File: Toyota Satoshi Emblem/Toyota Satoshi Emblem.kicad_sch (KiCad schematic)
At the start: 459 parts, among them J1 Conn_01x03_Male, J10 Conn_01x03_Male, J11 Letter Terminal, J12 Letter Terminal, J14 Power Port Terminal, J15 Raptor Term, J16 Serial Terminal, J17 S-Pads, J19 S-Pads, J2 Conn_01x03_Male, J20 S-Pads, J21 S-Pads, J22 Raptor Term, J23 Raptor Term, J24 Raptor Term, J3 Conn_01x03_Male, J4 Letter Terminal, J5 Letter Terminal, J6 Letter Terminal, J7 Letter Terminal, J8 Conn_01x03_Male, J9 Conn_01x03_Male, K1 FINDER-40.51, Q1 IRLR7843, Q10 IRLR7843, Q11 IRLR7843, Q12 2N3904, Q13 IRLR7843, Q14 IRLR7843, Q15 IRLR7843, Q16 2N3904, Q17 IRLR7843, Q18 IRLR7843, Q19 IRLR7843, Q2 IRLR7843, Q20 2N3904, Q21 IRLR7843, Q22 IRLR7843, Q23 IRLR7843, Q24 2N3904, Q25 IRLR7843, Q26 IRLR7843, Q27 IRLR7843, Q28 IRLR7843, Q29 IRLR7843, Q3 IRLR7843, Q30 IRLR7843, Q31 IRLR7843, Q32 IRLZ44N, Q33 IRLR7843, Q34 2N3904, Q35 IRLR7843, Q36 IRF4905, Q37 BC327, Q38 BC337, Q39 IRF4905, Q4 2N3904, Q5 IRLR7843, Q6 IRLR7843, Q7 IRLR7843, Q8 2N3904, Q9 IRLR7843, U5 L7805

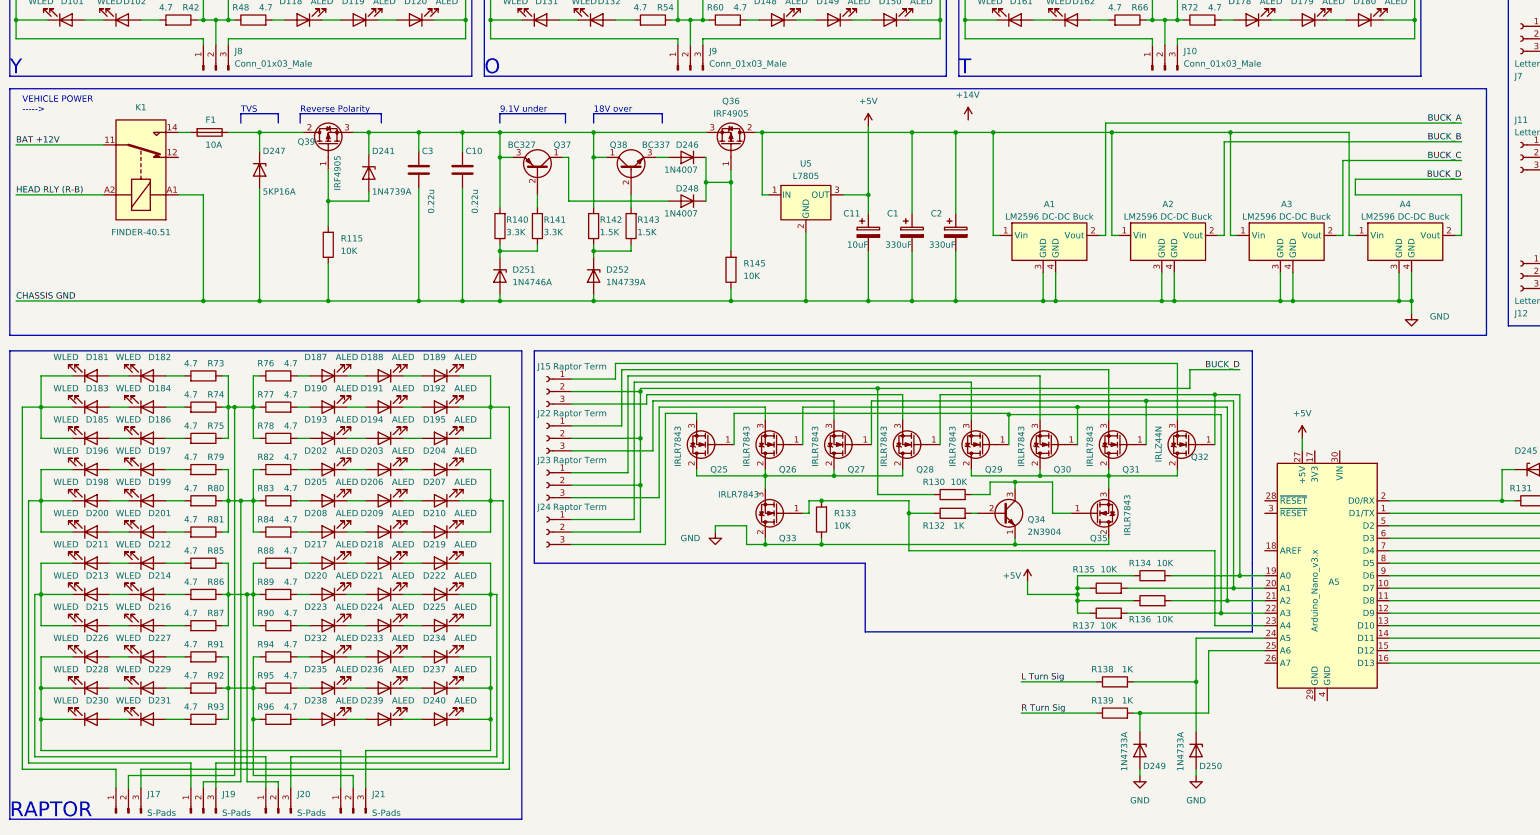
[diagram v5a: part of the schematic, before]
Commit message: v1.14
Control board pcb in the works
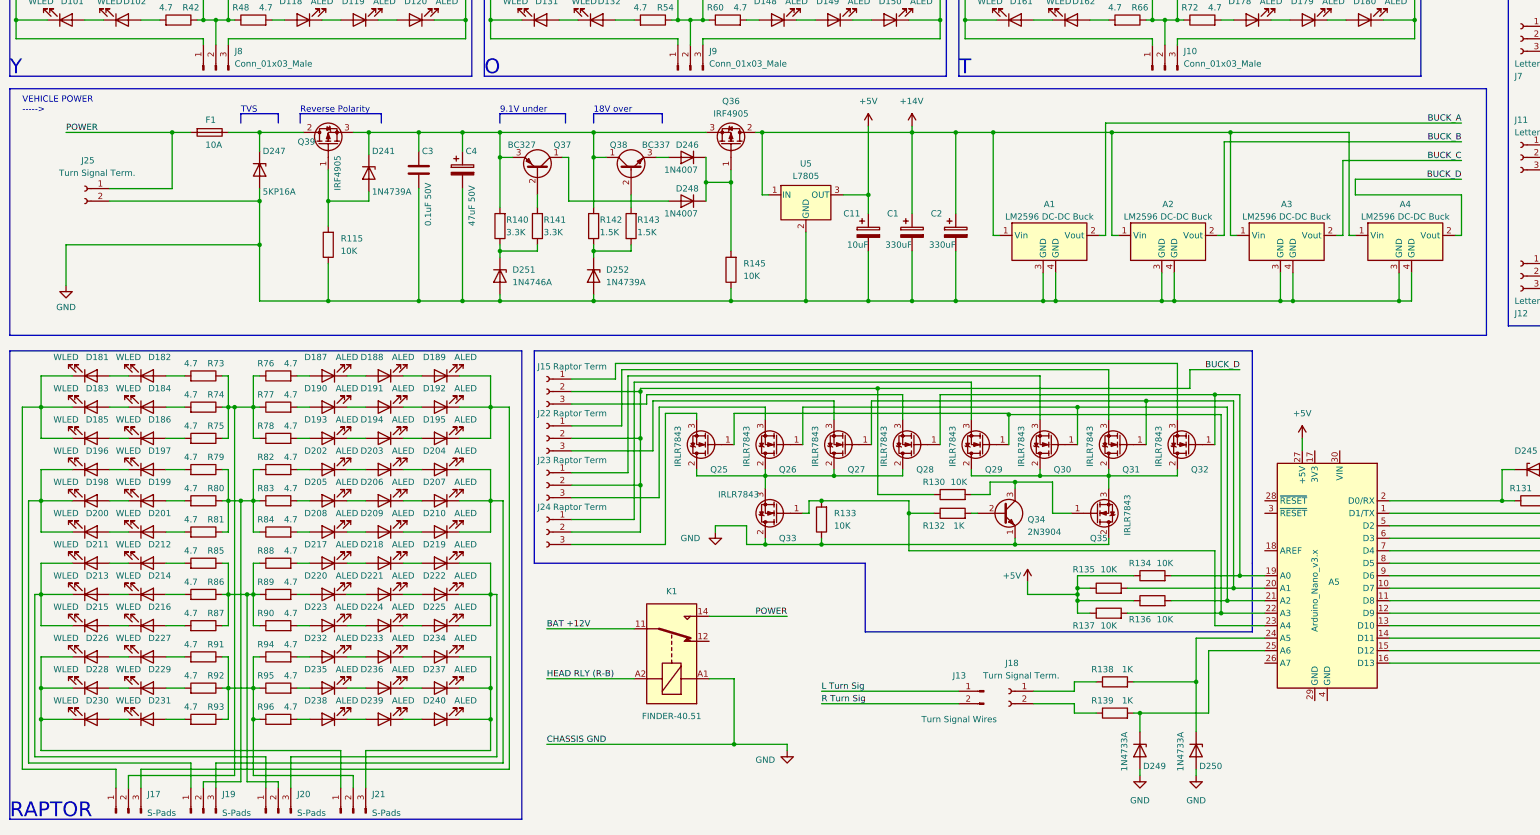
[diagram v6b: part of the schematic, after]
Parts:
- removed C10: 0.22u, symbol Device:C
- removed Q32: IRLZ44N, Package_TO_SOT_THT:TO-220-3_Vertical, symbol Transistor_FET:IRLZ44N
- added C4: 47uF 50V, Capacitor_THT:C_Radial_D5.0mm_H11.0mm_P2.00mm, symbol Device:C_Polarized
- added J13: Turn Signal Wires, TerminalBlock_Phoenix:TerminalBlock_Phoenix_MKDS-3-2-5.08_1x02_P5.08mm_Horizontal, symbol Connector:Conn_01x02_Male
- added J18, J25: Turn Signal Term., TerminalBlock_Phoenix:TerminalBlock_Phoenix_PT-1,5-2-5.0-H_1x02_P5.00mm_Horizontal, symbol Connector:Conn_01x02_Female
- added Q32: IRLR7843, afootprints:IRLR7843, symbol asymbols:IRLR7843
- C1, C2: footprint (none) -> Capacitor_THT:C_Radial_D8.0mm_H11.5mm_P3.50mm
- C11: footprint (none) -> Capacitor_THT:C_Radial_D4.0mm_H7.0mm_P1.50mm
- C3: value 0.22u -> 0.1uF 50V; footprint (none) -> Capacitor_THT:C_Disc_D7.5mm_W5.0mm_P5.00mm
- F1: footprint (none) -> afootprints:Univ_AUTO_Fuse
- J11, J12, J15, J22, J23, J24, J4, J5, J6, J7: footprint afootprints:PoiLee 3-Pin -> TerminalBlock_Phoenix:TerminalBlock_Phoenix_PT-1,5-3-5.0-H_1x03_P5.00mm_Horizontal
- J16: footprint afootprints:PoiLee 3-Pin -> TerminalBlock_Phoenix:TerminalBlock_Phoenix_PT-1,5-2-5.0-H_1x02_P5.00mm_Horizontal
- K1: now left out of the parts list
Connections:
- net +12V: now also A1.1 (Vin), A2.1 (Vin), A3.1 (Vin), A4.1 (Vin), C1.1, C2.1, Q36.2 (D), U5.1 (IN)
- net GND: now also C4.2, J25.2 (Pin_2)
- net L Turn Sig: now also J13.1 (Pin_1); no longer R138.1
- net R Turn Sig: now also J13.2 (Pin_2); no longer R139.1
- net at C3.1, D241.1 (K), Q36.3 (S)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: now also C4.1
- net POWER: now reaches F1.2, K1.14
- net POWER: now also J25.1 (Pin_1)
- net at Q29.2 (D), Q30.2 (D), Q31.2 (D)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: now also Q32.2 (D)
- net at A5.19 (A0), Q28.1 (G), R134.2: now also Q32.1 (G)
- net at J15.1 (Pin_1): now also Q32.3 (S)
- new net: J18.1 (Pin_1), R138.1
- new net: J18.2 (Pin_2), R139.1

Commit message: v1.15
Power sector of PCB mostly completed
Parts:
- A5: footprint afootprints:ArduinoNano -> Module:Arduino_Nano
- C1, C2: value 330uF -> 470uF
- D252: value 1N4739A -> 1N4738A
- Q12, Q16, Q20, Q24, Q34, Q4, Q8: footprint afootprints:2N3904SMD -> Package_TO_SOT_THT:TO-92_Inline
- R115, R145: footprint afootprints:THTresistor -> afootprints:1206 R
- R140, R141: value 3.3K -> 1K; footprint afootprints:THTresistor -> afootprints:1206 R
- R142, R143: value 1.5K -> 1K; footprint afootprints:THTresistor -> afootprints:1206 R

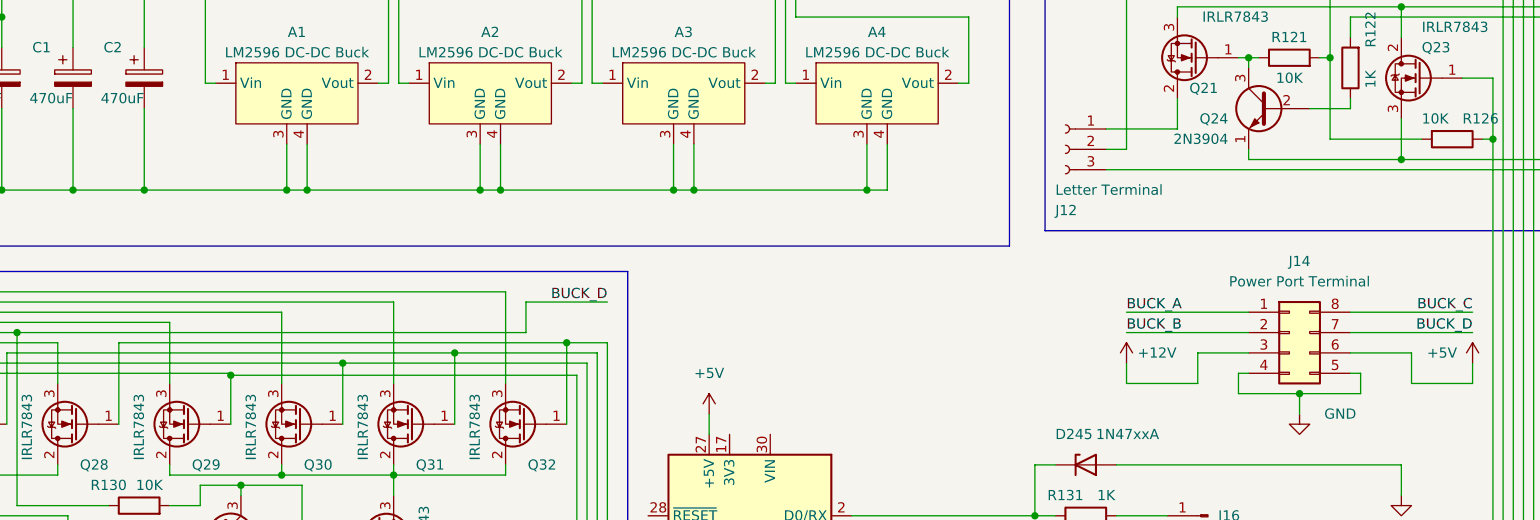
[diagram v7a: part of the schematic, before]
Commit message: v1.16
Realized critical errors were made when choosing trace widths. Control PCB will need to be redesigned
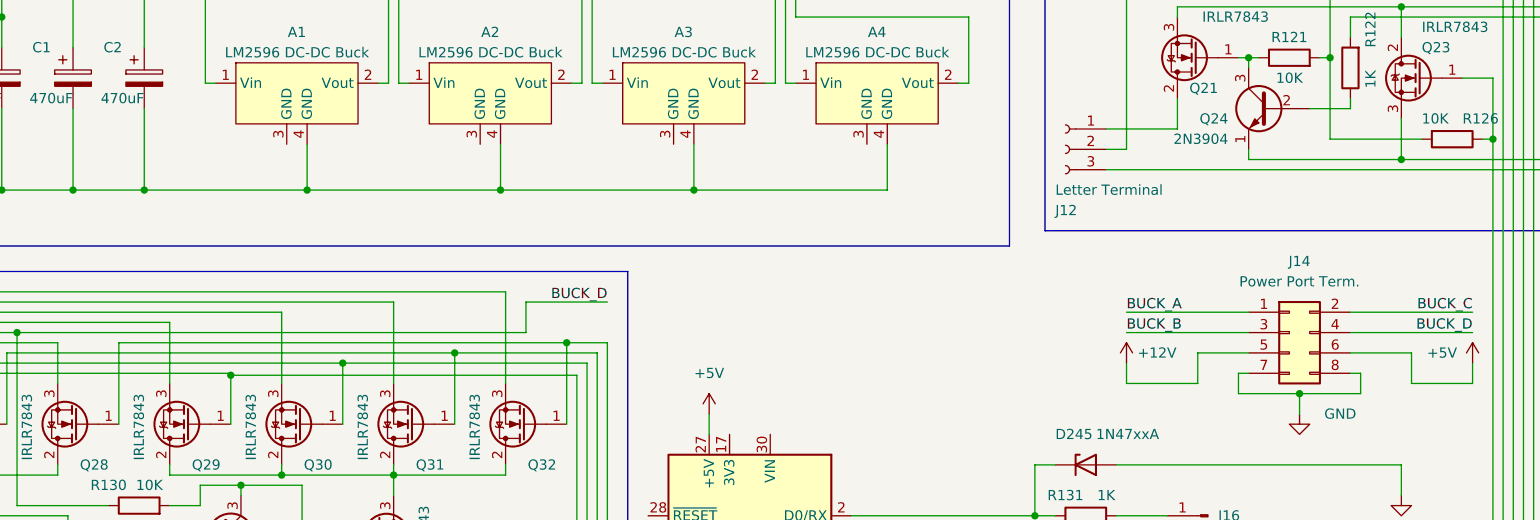
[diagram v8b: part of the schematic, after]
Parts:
- removed J14: Power Port Terminal, Connector_PinHeader_2.54mm:PinHeader_2x04_P2.54mm_Vertical, symbol Connector_Generic:Conn_02x04_Counter_Clockwise
- added J14: Power Port Term., Connector_PinHeader_2.54mm:PinHeader_2x04_P2.54mm_Vertical, symbol Connector_Generic:Conn_02x04_Odd_Even
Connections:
- net +12V: now also J14.5 (Pin_5)
- net +5V: now also J14.6 (Pin_6)
- net BUCK_A: now also J14.1 (Pin_1)
- net BUCK_B: now also J14.3 (Pin_3)
- net BUCK_C: now also J14.2 (Pin_2)
- net BUCK_D: now also J14.4 (Pin_4)
- net GND: now also J14.7 (Pin_7), J14.8 (Pin_8); no longer A1.3 (GND), A2.3 (GND), A3.3 (GND), A4.3 (GND)
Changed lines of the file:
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@@
     (title "Toyota Satoshi Emblem LED Board")
     (date "2022-02-16")
-    (rev "1.15")
+    (rev "1.16")
   )
   (junction (at 80.01 161.29) (diameter 0) (color 0 0 0 0)
@@
   (junction (at 98.425 127) (diameter 0) (color 0 0 0 0)
   )
-  (junction (at 225.425 161.29) (diameter 0) (color 0 0 0 0)
-  )
   (junction (at 143.51 198.755) (diameter 0) (color 0 0 0 0)
   )
@@
   (junction (at 345.44 96.52) (diameter 0) (color 0 0 0 0)
   )
-  (junction (at 297.815 161.29) (diameter 0) (color 0 0 0 0)
-  )
   (junction (at 156.21 52.07) (diameter 0) (color 0 0 0 0)
   )
@@
   (junction (at 300.99 85.09) (diameter 0) (color 0 0 0 0)
   )
-  (junction (at 273.685 161.29) (diameter 0) (color 0 0 0 0)
-  )
   (junction (at 300.99 39.37) (diameter 0) (color 0 0 0 0)
   )
@@
   (junction (at 16.51 33.02) (diameter 0) (color 0 0 0 0)
   )
-  (junction (at 249.555 161.29) (diameter 0) (color 0 0 0 0)
-  )
   (junction (at 151.1299 97.7899) (diameter 0) (color 0 0 0 0)
   )
@@
     (stroke (width 0) (type default) (color 0 0 0 0))
   )
-  (wire (pts (xy 227.965 161.29) (xy 225.425 161.29))
+  (wire (pts (xy 207.645 161.29) (xy 227.965 161.29))
     (stroke (width 0) (type default) (color 0 0 0 0))
   )
@@
     (stroke (width 0) (type default) (color 0 0 0 0))
   )
-  (wire (pts (xy 273.685 161.29) (xy 252.095 161.29))
+  (wire (pts (xy 252.095 161.29) (xy 276.225 161.29))
     (stroke (width 0) (type default) (color 0 0 0 0))
   )
@@
     (stroke (width 0) (type default) (color 0 0 0 0))
   )
-  (wire (pts (xy 249.555 161.29) (xy 227.965 161.29))
+  (wire (pts (xy 227.965 161.29) (xy 252.095 161.29))
     (stroke (width 0) (type default) (color 0 0 0 0))
   )
@@
     (stroke (width 0) (type default) (color 0 0 0 0))
   )
-  (wire (pts (xy 276.225 161.29) (xy 273.685 161.29))
-    (stroke (width 0) (type default) (color 0 0 0 0))
-  )
   (wire (pts (xy 336.55 41.91) (xy 364.49 41.91))
     (stroke (width 0) (type default) (color 0 0 0 0))
@@
     (stroke (width 0) (type default) (color 0 0 0 0))
   )
-  (wire (pts (xy 252.095 161.29) (xy 249.555 161.29))
-    (stroke (width 0) (type default) (color 0 0 0 0))
-  )
   (wire (pts (xy 410.21 29.21) (xy 410.21 38.1))
     (stroke (width 0) (type default) (color 0 0 0 0))
@@
     (stroke (width 0) (type default) (color 0 0 0 0))
   )
-  (wire (pts (xy 297.815 155.575) (xy 297.815 161.29))
-    (stroke (width 0) (type default) (color 0 0 0 0))
-  )
   (wire (pts (xy 165.1 210.82) (xy 168.91 210.82))
     (stroke (width 0) (type default) (color 0 0 0 0))
@@
     (stroke (width 0) (type default) (color 0 0 0 0))
   )
-  (wire (pts (xy 300.355 161.29) (xy 297.815 161.29))
+  (wire (pts (xy 276.225 161.29) (xy 300.355 161.29))
     (stroke (width 0) (type default) (color 0 0 0 0))
   )
@@
     (stroke (width 0) (type default) (color 0 0 0 0))
   )
-  (wire (pts (xy 249.555 155.575) (xy 249.555 161.29))
-    (stroke (width 0) (type default) (color 0 0 0 0))
-  )
   (wire (pts (xy 59.69 39.37) (xy 59.69 45.72))
     (stroke (width 0) (type default) (color 0 0 0 0))
@@
     (stroke (width 0) (type default) (color 0 0 0 0))
   )
-  (wire (pts (xy 225.425 161.29) (xy 207.645 161.29))
-    (stroke (width 0) (type default) (color 0 0 0 0))
-  )
   (wire (pts (xy 251.46 222.25) (xy 262.89 222.25))
     (stroke (width 0) (type default) (color 0 0 0 0))
@@
     (stroke (width 0) (type default) (color 0 0 0 0))
   )
-  (wire (pts (xy 273.685 155.575) (xy 273.685 161.29))
-    (stroke (width 0) (type default) (color 0 0 0 0))
-  )
   (wire (pts (xy 95.25 189.23) (xy 99.06 189.23))
     (stroke (width 0) (type default) (color 0 0 0 0))
@@
     (stroke (width 0) (type default) (color 0 0 0 0))
   )
-  (wire (pts (xy 225.425 155.575) (xy 225.425 161.29))
-    (stroke (width 0) (type default) (color 0 0 0 0))
-  )
   (wire (pts (xy 54.61 78.74) (xy 54.61 85.09))
     (stroke (width 0) (type default) (color 0 0 0 0))
@@
     (stroke (width 0) (type default) (color 0 0 0 0))
   )
-  (wire (pts (xy 297.815 161.29) (xy 276.225 161.29))
-    (stroke (width 0) (type default) (color 0 0 0 0))
-  )
   (wire (pts (xy 250.19 104.14) (xy 250.19 109.22))
     (stroke (width 0) (type default) (color 0 0 0 0))
@@
     (pin "2")
   )
+  (symbol (lib_id "Connector_Generic:Conn_02x04_Odd_Even") (at 350.52 179.07 0) (unit 1)
+    (in_bom yes) (on_board yes) (fields_autoplaced)
+    (property "Reference" "J14" (id 0) (at 351.79 170.18 0))
+    (property "Value" "Power Port Term." (id 1) (at 351.79 172.72 0))
+    (property "Footprint" "Connector_PinHeader_2.54mm:PinHeader_2x04_P2.54mm_Vertical" (id 2) (at 350.52 179.07 0)
+      (effects (font (size 1.27 1.27)) hide)
+    )
+    (property "Datasheet" "~" (id 3) (at 350.52 179.07 0)
+      (effects (font (size 1.27 1.27)) hide)
+    )
+    (pin "1")
+    (pin "2")
+    (pin "3")
+    (pin "4")
+    (pin "5")
+    (pin "6")
+    (pin "7")
+    (pin "8")
+  )
   (symbol (lib_id "asymbols:IRLR7843") (at 168.91 204.47 180) (unit 1)
     (in_bom yes) (on_board yes)
@@
     (pin "2")
   )
-  (symbol (lib_id "Connector_Generic:Conn_02x04_Counter_Clockwise") (at 350.52 179.07 0) (unit 1)
-    (in_bom yes) (on_board yes)
-    (property "Reference" "J14" (id 0) (at 351.79 170.18 0))
-    (property "Value" "Power Port Terminal" (id 1) (at 351.79 172.72 0))
-    (property "Footprint" "Connector_PinHeader_2.54mm:PinHeader_2x04_P2.54mm_Vertical" (id 2) (at 350.52 179.07 0)
-      (effects (font (size 1.27 1.27)) hide)
-    )
-    (property "Datasheet" "~" (id 3) (at 350.52 179.07 0)
-      (effects (font (size 1.27 1.27)) hide)
-    )
-    (pin "1")
-    (pin "2")
-    (pin "3")
-    (pin "4")
-    (pin "5")
-    (pin "6")
-    (pin "7")
-    (pin "8")
-  )
   (symbol (lib_id "Device:LED") (at 134.6199 91.4399 0) (mirror x) (unit 1)
     (in_bom yes) (on_board yes)
@@
       (reference "J13") (unit 1) (value "Turn Signal Wires") (footprint "TerminalBlock_Phoenix:TerminalBlock_Phoenix_MKDS-3-2-5.08_1x02_P5.08mm_Horizontal")
     )
-    (path "/417f2635-910a-41cc-9792-e035b7a58780"
-      (reference "J14") (unit 1) (value "Power Port Terminal") (footprint "Connector_PinHeader_2.54mm:PinHeader_2x04_P2.54mm_Vertical")
+    (path "/2df48a86-22f1-44cb-9e6e-283f0b58062e"
+      (reference "J14") (unit 1) (value "Power Port Term.") (footprint "Connector_PinHeader_2.54mm:PinHeader_2x04_P2.54mm_Vertical")
     )
     (path "/ffd2b1e5-e989-4de9-b2f3-45fff7d0f248"
